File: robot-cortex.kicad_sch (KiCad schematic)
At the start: 26 parts, among them J1 USB4110GFA, Q1 SS8050-G, Q2 SS8050-G, U1 DF52-4S-0.8H(21), U2 ESP32-WROOM-32E-H4, U3 DF52-5S-0.8H(21), U4 DF52-4S-0.8H(21), U5 CP2102N-A02-GQFN24R

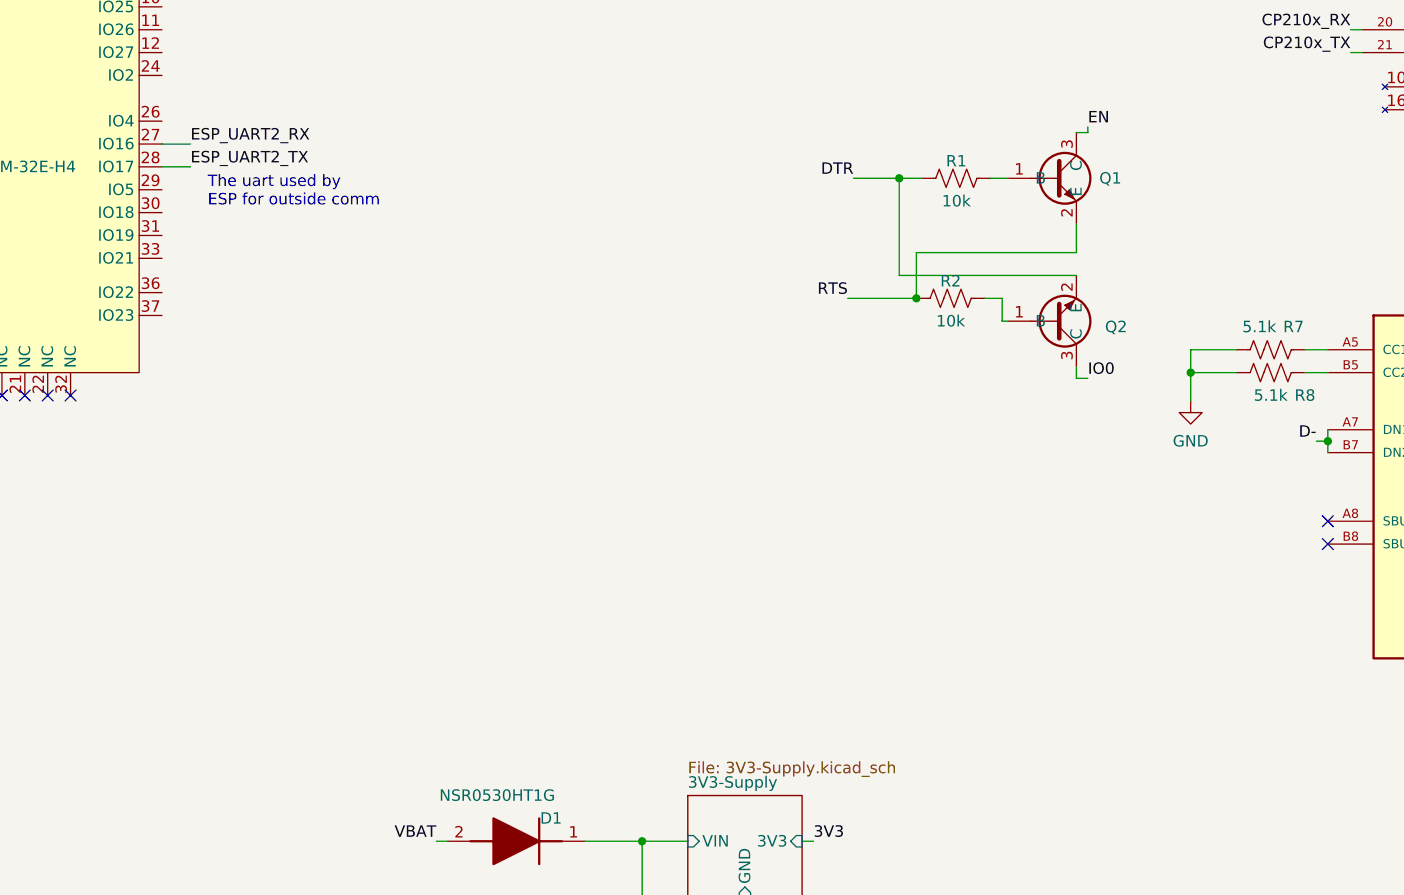
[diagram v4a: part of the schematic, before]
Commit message: added tvs diodes, schematic review. Probably gonna axe the external uart for this one
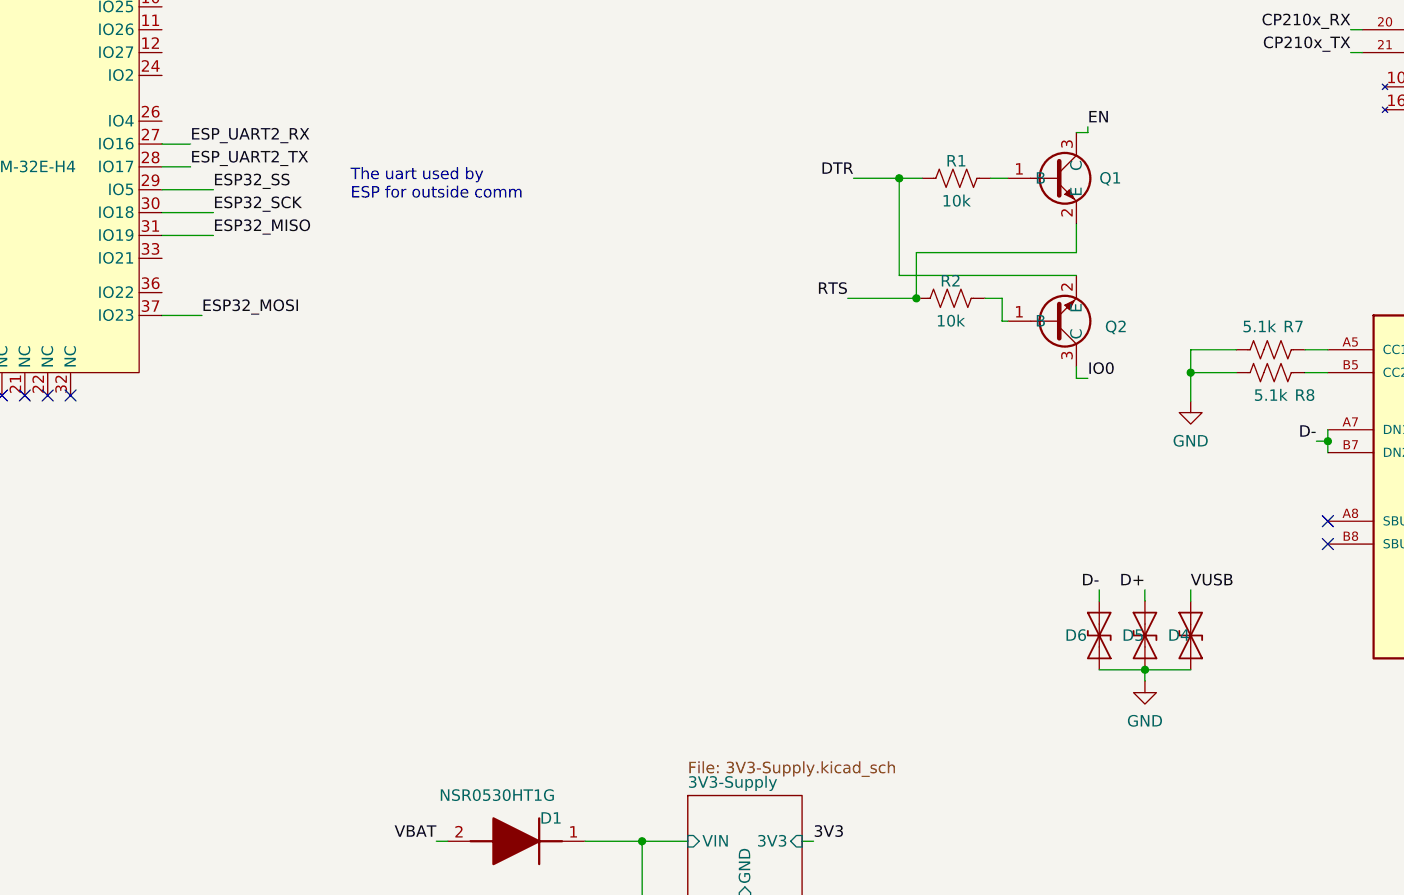
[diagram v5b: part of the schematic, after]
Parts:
- added D4, D5, D6: ESD9B3.3ST5G, robot-cortex:D_SOD-923, symbol robot-cortex:ESD9B3.3ST5G
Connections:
- net D+: now also D5.2 (A2)
- net D-: now also D6.2 (A2)
- net GND: now also D4.1 (A1), D5.1 (A1), D6.1 (A1)
- net VUSB: now also D4.2 (A2)
- net ESP32_SS: now reaches U2.29 (IO5)
- net ESP32_SCK: now reaches U2.30 (IO18)
- net ESP32_MISO: now reaches U2.31 (IO19)
- net ESP32_MOSI: now reaches U2.37 (IO23)
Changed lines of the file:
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@@
   (junction (at 236.22 134.62) (diameter 0) (color 0 0 0 0)
+  )
+  (junction (at 180.34 138.43) (diameter 0) (color 0 0 0 0)
   )
   (junction (at 99.314 34.417) (diameter 0) (color 0 0 0 0)
@@
     (stroke (width 0) (type default))
   )
+  (wire (pts (xy 76.835 90.17) (xy 71.12 90.17))
+    (stroke (width 0) (type default))
+  )
   (wire (pts (xy 257.81 29.21) (xy 250.19 29.21))
     (stroke (width 0) (type default))
@@
     (stroke (width 0) (type default))
   )
+  (wire (pts (xy 180.34 139.7) (xy 180.34 138.43))
+    (stroke (width 0) (type default))
+  )
   (wire (pts (xy 29.21 140.97) (xy 29.21 142.24))
     (stroke (width 0) (type default))
@@
     (stroke (width 0) (type default))
   )
+  (wire (pts (xy 75.565 99.06) (xy 71.12 99.06))
+    (stroke (width 0) (type default))
+  )
   (wire (pts (xy 43.18 143.51) (xy 43.18 130.81))
     (stroke (width 0) (type default))
@@
     (stroke (width 0) (type default))
   )
+  (wire (pts (xy 175.26 129.54) (xy 175.26 130.81))
+    (stroke (width 0) (type default))
+  )
   (wire (pts (xy 250.19 31.75) (xy 250.19 34.29))
     (stroke (width 0) (type default))
@@
     (stroke (width 0) (type default))
   )
+  (wire (pts (xy 175.26 138.43) (xy 180.34 138.43))
+    (stroke (width 0) (type default))
+  )
   (wire (pts (xy 34.29 44.45) (xy 35.56 44.45))
     (stroke (width 0) (type default))
@@
     (stroke (width 0) (type default))
   )
+  (wire (pts (xy 180.34 138.43) (xy 185.42 138.43))
+    (stroke (width 0) (type default))
+  )
   (wire (pts (xy 24.13 26.67) (xy 25.4 26.67))
     (stroke (width 0) (type default))
@@
     (stroke (width 0) (type default))
   )
+  (wire (pts (xy 76.835 85.09) (xy 71.12 85.09))
+    (stroke (width 0) (type default))
+  )
   (wire (pts (xy 22.86 46.99) (xy 29.21 46.99))
     (stroke (width 0) (type default))
@@
     (stroke (width 0) (type default))
   )
+  (wire (pts (xy 185.42 129.54) (xy 185.42 130.81))
+    (stroke (width 0) (type default))
+  )
   (wire (pts (xy 34.29 74.93) (xy 35.56 74.93))
     (stroke (width 0) (type default))
@@
     (stroke (width 0) (type default))
   )
+  (wire (pts (xy 180.34 129.54) (xy 180.34 130.81))
+    (stroke (width 0) (type default))
+  )
   (wire (pts (xy 43.18 171.45) (xy 43.18 158.75))
+    (stroke (width 0) (type default))
+  )
+  (wire (pts (xy 76.835 87.63) (xy 71.12 87.63))
     (stroke (width 0) (type default))
   )
@@
     (effects (font (size 1.27 1.27)) (justify left bottom))
   )
-  (text "The uart used by\nESP for outside comm\n" (at 76.2 87.122 0)
+  (text "The uart used by\nESP for outside comm\n" (at 92.075 86.36 0)
     (effects (font (size 1.27 1.27)) (justify left bottom))
   )
@@
     (effects (font (size 1.27 1.27)) (justify right bottom))
   )
+  (label "ESP32_SCK" (at 76.835 87.63 0) (fields_autoplaced)
+    (effects (font (size 1.27 1.27)) (justify left bottom))
+  )
   (label "EN" (at 24.13 26.67 180) (fields_autoplaced)
     (effects (font (size 1.27 1.27)) (justify right bottom))
@@
     (effects (font (size 1.27 1.27)) (justify right bottom))
   )
+  (label "ESP32_SS" (at 76.835 85.09 0) (fields_autoplaced)
+    (effects (font (size 1.27 1.27)) (justify left bottom))
+  )
   (label "RTS" (at 147.32 97.155 180) (fields_autoplaced)
     (effects (font (size 1.27 1.27)) (justify right bottom))
@@
     (effects (font (size 1.27 1.27)) (justify right bottom))
   )
+  (label "ESP32_MOSI" (at 75.565 99.06 0) (fields_autoplaced)
+    (effects (font (size 1.27 1.27)) (justify left bottom))
+  )
   (label "3V3" (at 143.51 157.48 0) (fields_autoplaced)
     (effects (font (size 1.27 1.27)) (justify left bottom))
@@
     (effects (font (size 1.27 1.27)) (justify right bottom))
   )
+  (label "D+" (at 180.34 129.54 180) (fields_autoplaced)
+    (effects (font (size 1.27 1.27)) (justify right bottom))
+  )
   (label "RTS" (at 203.2 54.61 180) (fields_autoplaced)
     (effects (font (size 1.27 1.27)) (justify right bottom))
@@
     (effects (font (size 1.27 1.27)) (justify left bottom))
   )
+  (label "VUSB" (at 185.42 129.54 0) (fields_autoplaced)
+    (effects (font (size 1.27 1.27)) (justify left bottom))
+  )
   (label "ESP_UART2_TX" (at 74.295 82.55 0) (fields_autoplaced)
     (effects (font (size 1.27 1.27)) (justify left bottom))
@@
     (effects (font (size 1.27 1.27)) (justify right bottom))
   )
+  (label "ESP32_MISO" (at 76.835 90.17 0) (fields_autoplaced)
+    (effects (font (size 1.27 1.27)) (justify left bottom))
+  )
   (label "EN" (at 34.29 46.99 180) (fields_autoplaced)
     (effects (font (size 1.27 1.27)) (justify right bottom))
@@
   )
   (label "CP210x_TX" (at 203.2 69.85 180) (fields_autoplaced)
+    (effects (font (size 1.27 1.27)) (justify right bottom))
+  )
+  (label "D-" (at 175.26 129.54 180) (fields_autoplaced)
     (effects (font (size 1.27 1.27)) (justify right bottom))
   )
@@
     )
   )
+  (symbol (lib_id "power:GND") (at 180.34 139.7 0) (unit 1)
+    (in_bom yes) (on_board yes) (dnp no) (fields_autoplaced)
+    (property "Reference" "#PWR023" (at 180.34 146.05 0)
+      (effects (font (size 1.27 1.27)) hide)
+    )
+    (property "Value" "GND" (at 180.34 144.145 0)
+      (effects (font (size 1.27 1.27)))
+    )
+    (property "Footprint" "" (at 180.34 139.7 0)
+      (effects (font (size 1.27 1.27)) hide)
+    )
+    (property "Datasheet" "" (at 180.34 139.7 0)
+      (effects (font (size 1.27 1.27)) hide)
+    )
+    (pin "1")
+    (instances
+      (project "robot-cortex"
+        (path "/19e4cb9f-d0a4-4ce0-8aa4-5fe95563dc37"
+          (reference "#PWR023") (unit 1)
+        )
+      )
+    )
+  )
   (symbol (lib_id "robot-cortex:DF52-4S-0.8H(21)") (at 38.1 137.16 0) (unit 1)
     (in_bom yes) (on_board yes) (dnp no) (fields_autoplaced)
@@
     )
   )
+  (symbol (lib_id "robot-cortex:ESD9B3.3ST5G") (at 180.34 134.62 90) (unit 1)
+    (in_bom yes) (on_board yes) (dnp no)
+    (property "Reference" "D5" (at 177.8 134.62 90)
+      (effects (font (size 1.27 1.27)) (justify right))
+    )
+    (property "Value" "ESD9B3.3ST5G" (at 180.34 142.24 90)
+      (effects (font (size 1.27 1.27)) (justify right) hide)
+    )
+    (property "Footprint" "robot-cortex:D_SOD-923" (at 175.26 132.08 0)
+      (effects (font (size 1.27 1.27)) hide)
+    )
+    (property "Datasheet" "https://www.onsemi.com/pub/Collateral/ESD9B-D.PDF" (at 175.26 132.08 0)
+      (effects (font (size 1.27 1.27)) hide)
+    )
+    (pin "1")
+    (pin "2")
+    (instances
+      (project "robot-cortex"
+        (path "/19e4cb9f-d0a4-4ce0-8aa4-5fe95563dc37"
+          (reference "D5") (unit 1)
+        )
+      )
+    )
+  )
   (symbol (lib_id "power:GND") (at 30.48 170.18 0) (unit 1)
     (in_bom yes) (on_board yes) (dnp no) (fields_autoplaced)
@@
         (path "/19e4cb9f-d0a4-4ce0-8aa4-5fe95563dc37"
           (reference "C1") (unit 1)
+        )
+      )
+    )
+  )
+  (symbol (lib_id "robot-cortex:ESD9B3.3ST5G") (at 185.42 134.62 90) (unit 1)
+    (in_bom yes) (on_board yes) (dnp no)
+    (property "Reference" "D4" (at 182.88 134.62 90)
+      (effects (font (size 1.27 1.27)) (justify right))
+    )
+    (property "Value" "ESD9B3.3ST5G" (at 186.69 140.97 90)
+      (effects (font (size 1.27 1.27)) (justify right) hide)
+    )
+    (property "Footprint" "robot-cortex:D_SOD-923" (at 180.34 132.08 0)
+      (effects (font (size 1.27 1.27)) hide)
+    )
+    (property "Datasheet" "https://www.onsemi.com/pub/Collateral/ESD9B-D.PDF" (at 180.34 132.08 0)
+      (effects (font (size 1.27 1.27)) hide)
+    )
+    (pin "1")
+    (pin "2")
+    (instances
+      (project "robot-cortex"
+        (path "/19e4cb9f-d0a4-4ce0-8aa4-5fe95563dc37"
+          (reference "D4") (unit 1)
         )
       )
@@
         )
       )
+    )
+  )
+  (symbol (lib_id "robot-cortex:ESD9B3.3ST5G") (at 175.26 134.62 90) (unit 1)
+    (in_bom yes) (on_board yes) (dnp no)
+    (property "Reference" "D6" (at 171.45 134.62 90)
+      (effects (font (size 1.27 1.27)) (justify right))
+    )
+    (property "Value" "ESD9B3.3ST5G" (at 177.8 135.89 90)
+      (effects (font (size 1.27 1.27)) (justify right) hide)
+    )
+    (property "Footprint" "robot-cortex:D_SOD-923" (at 170.18 132.08 0)
+      (effects (font (size 1.27 1.27)) hide)
+    )
+    (property "Datasheet" "https://www.onsemi.com/pub/Collateral/ESD9B-D.PDF" (at 170.18 132.08 0)
+      (effects (font (size 1.27 1.27)) hide)
+    )
+    (pin "1")
+    (pin "2")
+    (instances
+      (project "robot-cortex"
+        (path "/19e4cb9f-d0a4-4ce0-8aa4-5fe95563dc37"
+          (reference "D6") (unit 1)
+        )
+      )

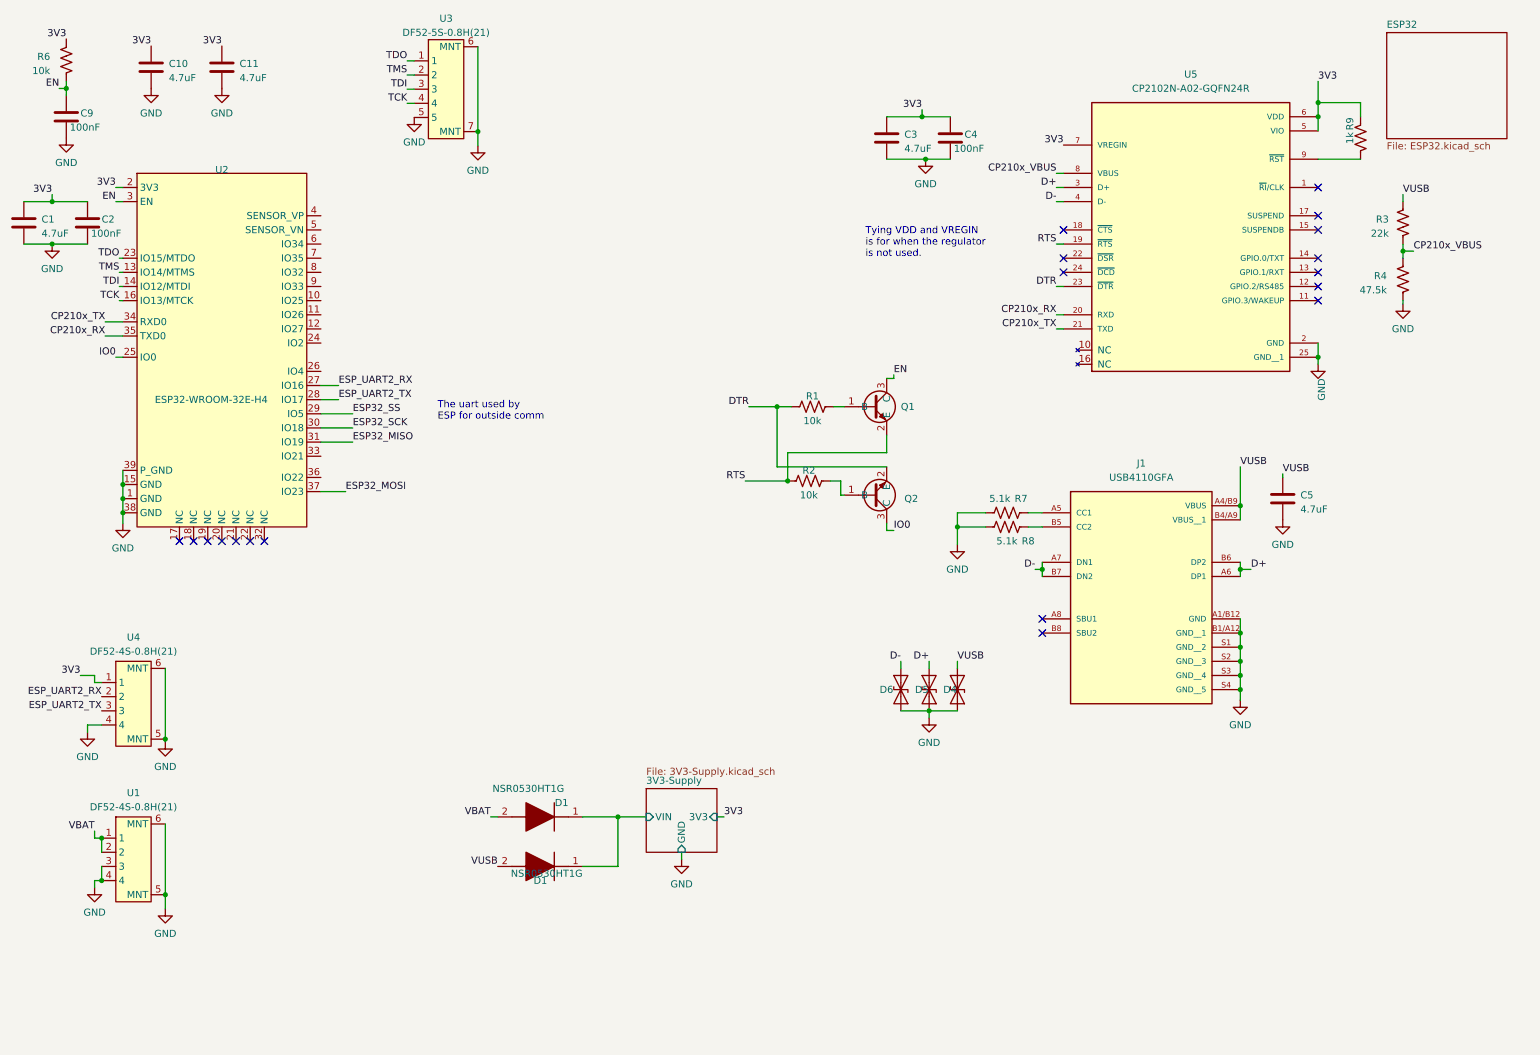
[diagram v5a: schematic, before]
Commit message: moved esp32 to heirarchichalca
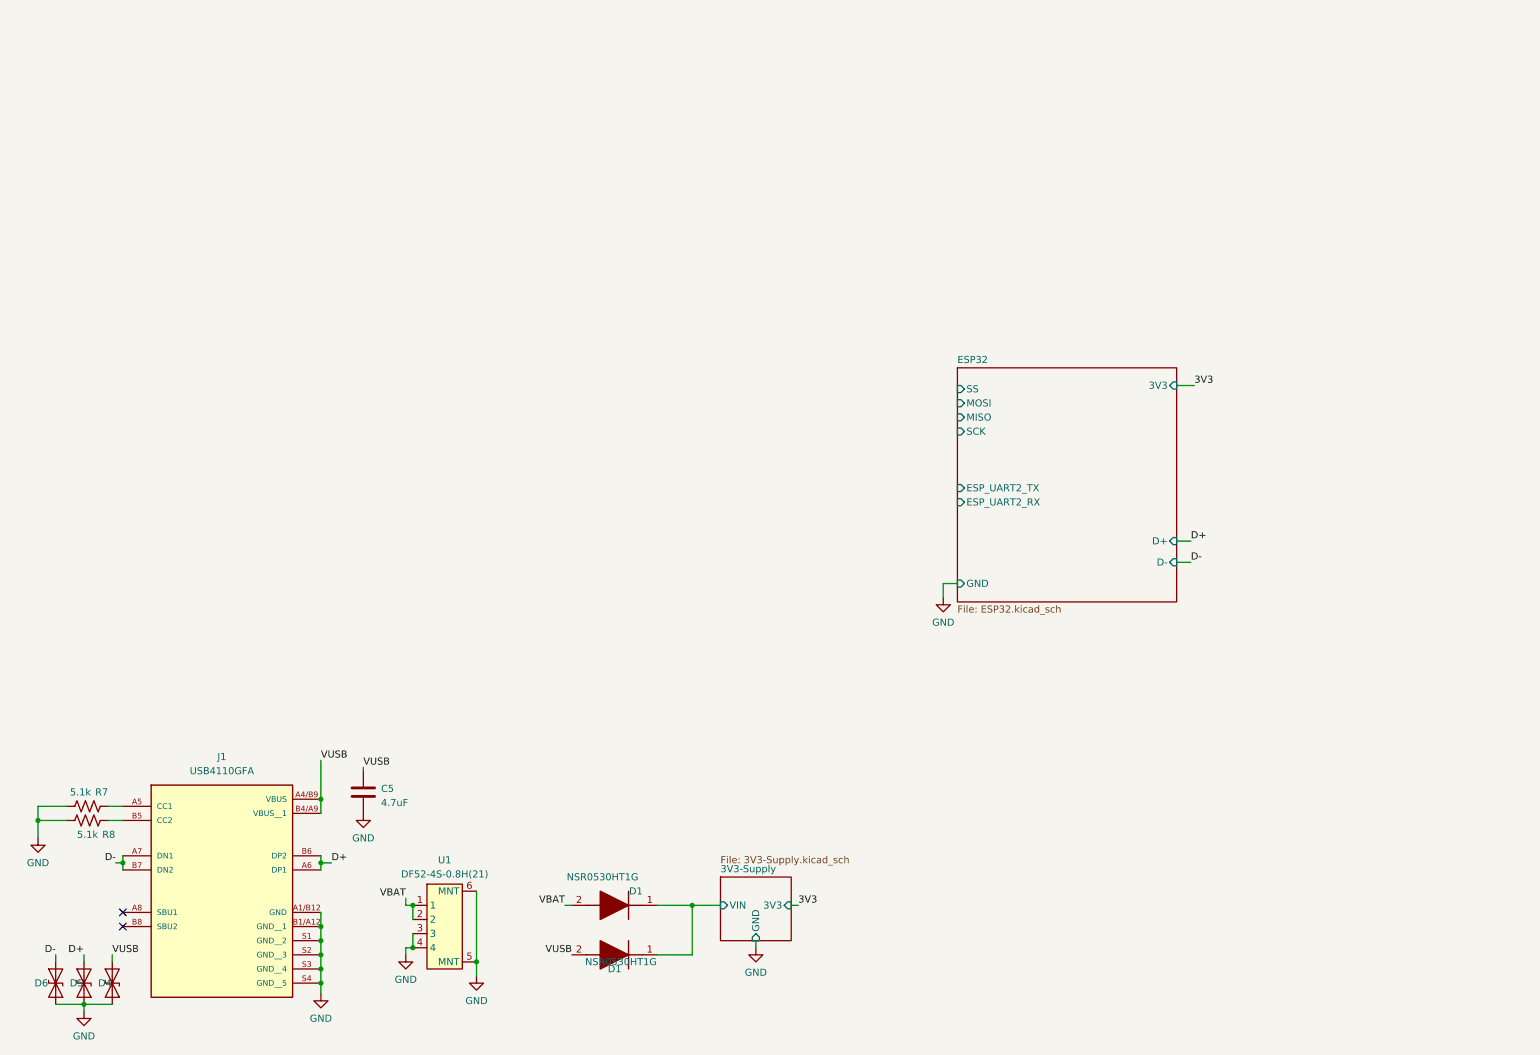
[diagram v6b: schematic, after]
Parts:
- removed C1, C10, C11, C3: 4.7uF, robot-cortex:C_0603_1608Metric, symbol robot-cortex:Capacitor
- removed C2, C4, C9: 100nF, robot-cortex:C_0402_1005Metric, symbol robot-cortex:Capacitor
- removed Q1, Q2: SS8050-G, robot-cortex:SOT-23-3, symbol robot-cortex:SS8050-G
- removed R1, R2, R6: 10k, robot-cortex:R_0402_1005Metric, symbol robot-cortex:Resistor
- removed R3: 22k, robot-cortex:R_0402_1005Metric, symbol robot-cortex:Resistor
- removed R4: 47.5k, robot-cortex:R_0402_1005Metric, symbol robot-cortex:Resistor
- removed R9: 1k, robot-cortex:R_0402_1005Metric, symbol robot-cortex:Resistor
- removed U2: ESP32-WROOM-32E-H4, robot-cortex:ESP32-WROOM-32, symbol robot-cortex:ESP32-WROOM-32E-H4
- removed U3: DF52-5S-0.8H(21), robot-cortex:DF52-5S-0.8H(21), symbol robot-cortex:DF52-5S-0.8H(21)
- removed U4: DF52-4S-0.8H(21), robot-cortex:DF52-4S-0.8H(21), symbol robot-cortex:DF52-4S-0.8H(21)
- removed U5: CP2102N-A02-GQFN24R, robot-cortex:QFN50P400X400X80-25N, symbol robot-cortex:CP2102N-A02-GQFN24R
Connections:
- no-connect marks 19 -> 2
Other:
- sheet ESP32 ports: added 3V3, D+, D-, ESP_UART2_RX, ESP_UART2_TX, GND, MISO, MOSI, SCK, SS; removed none
- note removed: "The uart used by ESP for outside comm"
- note removed: "Tying VDD and VREGIN is for when the regulator is not used."
- moved on the sheet: C5, D1, D4, D5, D6, J1, R7, R8, U1
